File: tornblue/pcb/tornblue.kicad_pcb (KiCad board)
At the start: 2 copper layers, 140.7 x 102.9 mm, 80 parts, among them J1 BATT, J2 SWD, J3 BREAKOUT, J4 USB C - USB2.0, J5 BATT_PIN, Q1 AO3401A, Q2 AO3401A, SW1 SW_Push, SW10 SW_Push, SW11 SW_Push, SW12 SW_Push, SW13 SW_Push, SW14 SW_Push, SW15 SW_Push, SW16 SW_Push, SW17 SW_Push, SW18 SW_Push, SW19 EC11, SW2 SW_Push, SW20 SW_Push, SW21 SW_Push, SW22 EC11, SW23 RST, SW24 SW_SPST, SW3 SW_Push, SW4 SW_Push, SW5 SW_Push, SW6 SW_Push, SW7 SW_Push, SW8 SW_Push, SW9 SW_Push, U1 XC6220, U2 TP4056, U3 nRF52840_holyiot_18010, U4 SRV05-4

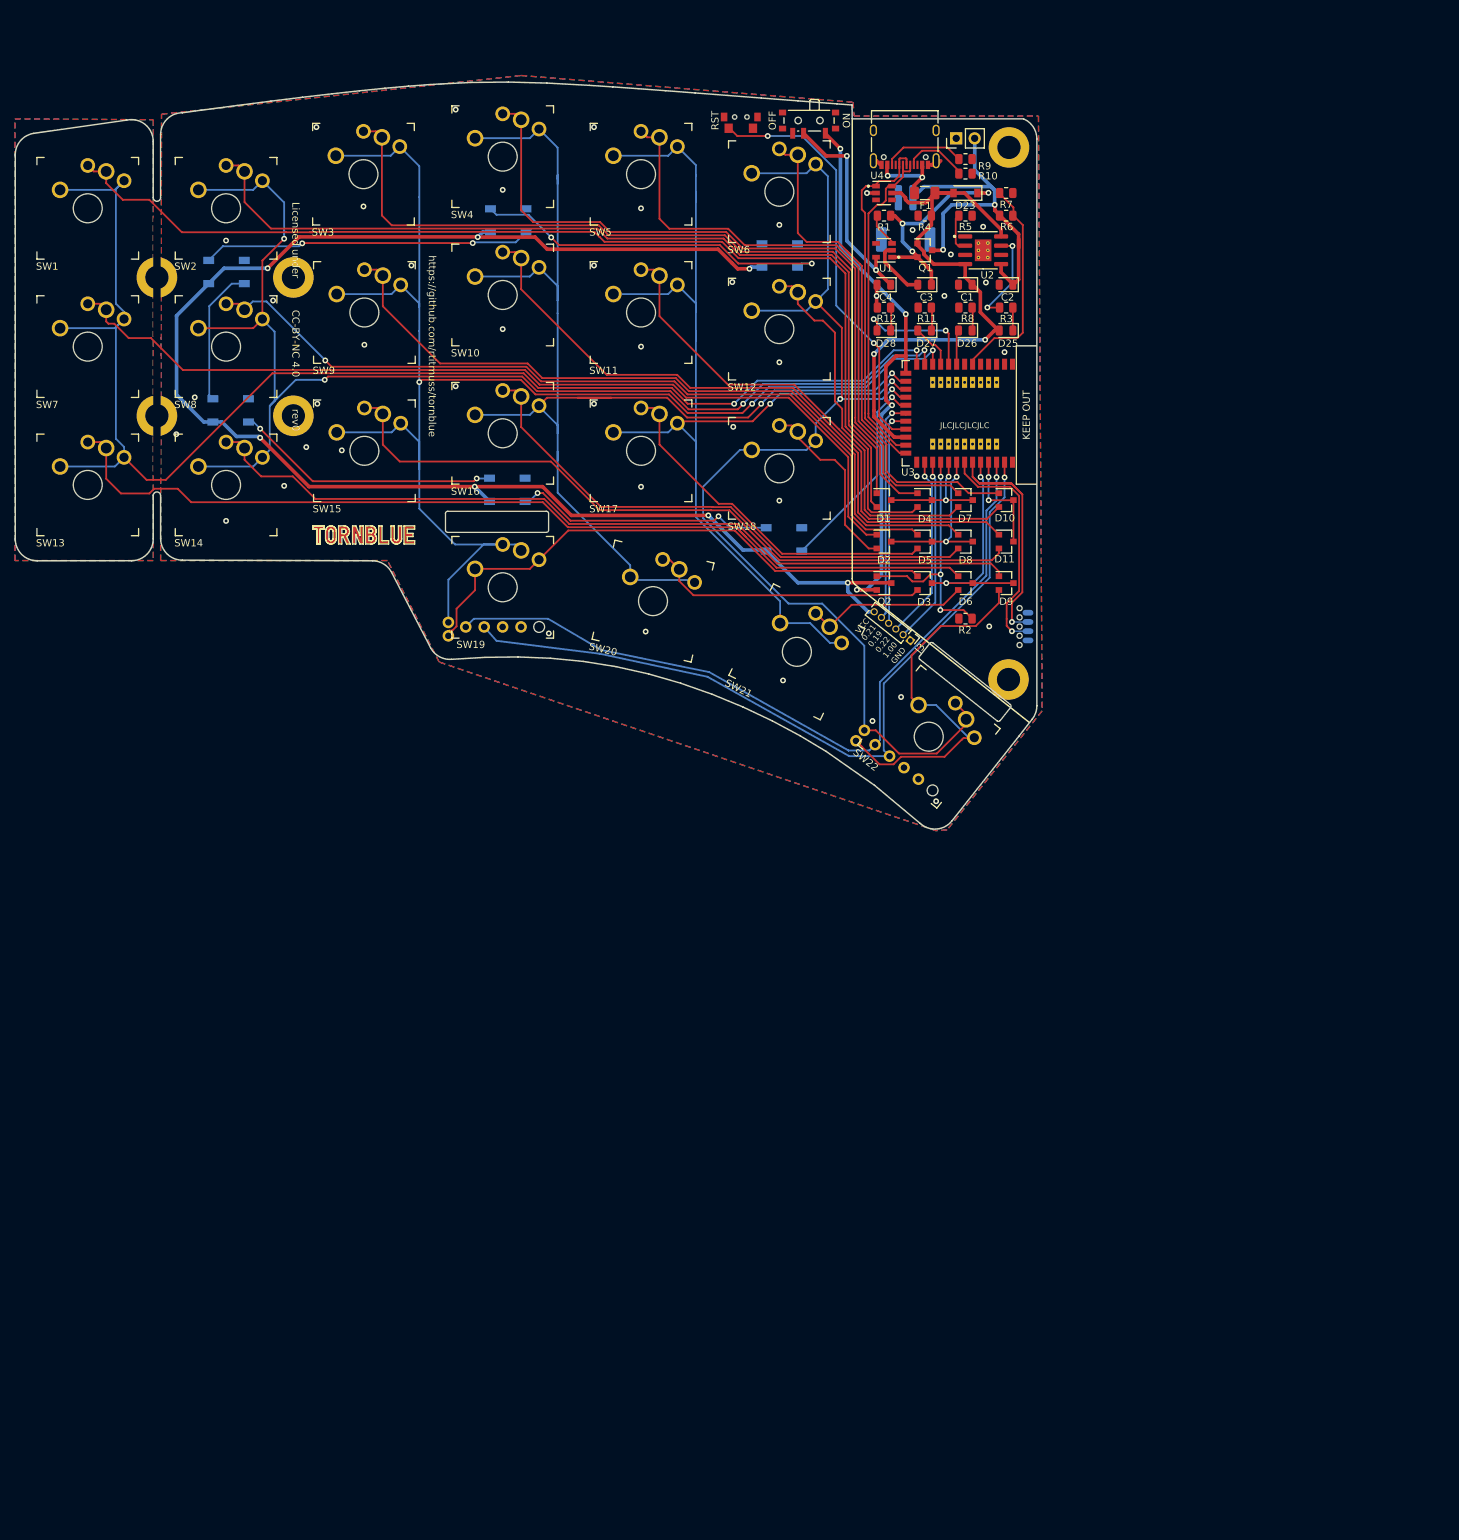
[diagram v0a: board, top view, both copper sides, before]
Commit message: Add right edgecuts
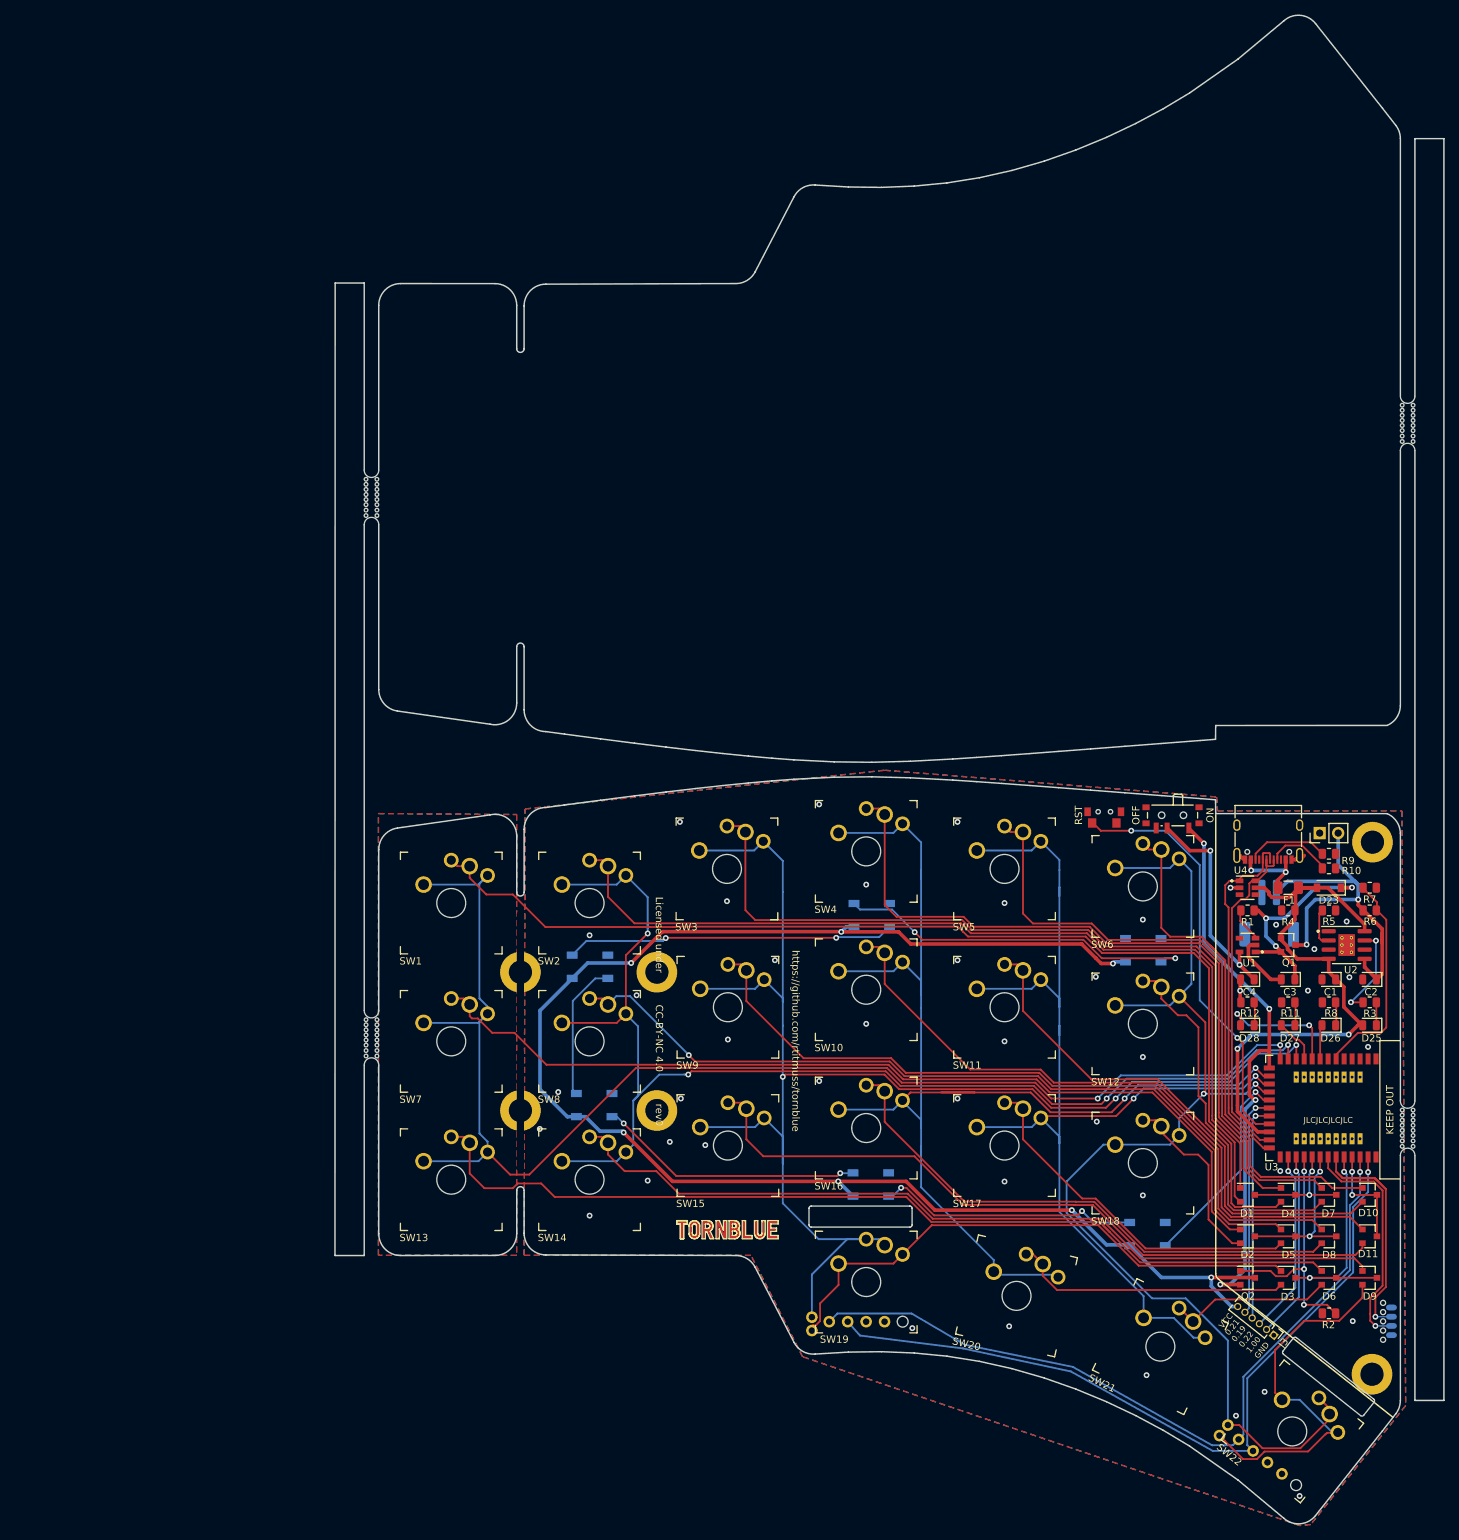
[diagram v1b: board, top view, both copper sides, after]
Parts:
- added mouse-bite-5mm-slot: VAL**, tornblue:mouse-bite-5mm-slot, F.Cu at (272.8, 94.3)
- added mouse-bite-5mm-slot: VAL**, tornblue:mouse-bite-5mm-slot, F.Cu at (272.8, 191.3)
- added mouse-bite-5mm-slot: VAL**, tornblue:mouse-bite-5mm-slot, F.Cu at (130.1, 104.5)
- added mouse-bite-5mm-slot: VAL**, tornblue:mouse-bite-5mm-slot, F.Cu at (130.1, 178.9)
- moved D3 108.0 mm to (256.4, 211.9)
- moved F1 108.0 mm to (256.4, 158.2)
- moved H1 108.0 mm to (268.0, 151.9)
- moved Q1 108.0 mm to (256.4, 166.1)
- moved R11 108.0 mm to (256.4, 174.0)
- moved D13 108.0 mm to (198.9, 199.1)
- moved D15 108.0 mm to (236.4, 166.8)
- moved D16 108.0 mm to (199.0, 162.0)
- moved D17 108.0 mm to (160.2, 169.1)
- moved D23 108.0 mm to (262.0, 158.2)
- moved D4 108.0 mm to (256.4, 200.5)
- moved D5 108.0 mm to (256.4, 206.2)
- moved D6 108.0 mm to (262.0, 211.9)
- moved D9 108.0 mm to (267.6, 211.9)
- moved H2 108.0 mm to (267.9, 225.2)
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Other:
- board size 140.7 x 102.9 mm -> 152.7 x 207.8 mm

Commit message: Add right schematic
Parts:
- added C5: 10uF, Diode_SMD:D_0805_2012Metric, F.Cu at (374.5, 130.2)
- added C6: 10uF, Diode_SMD:D_0805_2012Metric, F.Cu at (374.5, 133.2)
- added C7: 10uF, Diode_SMD:D_0805_2012Metric, F.Cu at (383.0, 125.3)
- added C8: 10uF, Diode_SMD:D_0805_2012Metric, F.Cu at (427.8, 79.5)
- added D18: BLUE, LED_SMD:LED_0805_2012Metric, F.Cu at (429.0, 75.2)
- added D19: BAV70_Small, Package_TO_SOT_SMD:SOT-23, F.Cu at (335.6, 133.9)
- added D20: BAV70_Small, Package_TO_SOT_SMD:SOT-23, F.Cu at (391.4, 116.4)
- added D21: BAV70_Small, Package_TO_SOT_SMD:SOT-23, F.Cu at (395.9, 111.8)
- added D22: BAV70_Small, Package_TO_SOT_SMD:SOT-23, F.Cu at (410.5, 96.5)
- added D24: B5819W, Diode_SMD:D_SOD-123, F.Cu at (306.3, 133.3)
- added D29: BAV70_Small, Package_TO_SOT_SMD:SOT-23, F.Cu at (415.0, 92.0)
- added D30: BAV70_Small, Package_TO_SOT_SMD:SOT-23, F.Cu at (417.5, 87.4)
- added D31: BAV70_Small, Package_TO_SOT_SMD:SOT-23, F.Cu at (410.5, 92.0)
- added D32: BAV70_Small, Package_TO_SOT_SMD:SOT-23, F.Cu at (391.4, 111.8)
- added D33: BAV70_Small, Package_TO_SOT_SMD:SOT-23, F.Cu at (370.0, 131.0)
- added D34: BAV70_Small, Package_TO_SOT_SMD:SOT-23, F.Cu at (383.0, 118.5)
- added D35: BAV70_Small, Package_TO_SOT_SMD:SOT-23, F.Cu at (340.1, 133.9)
- added D36: WS2812B, LED_SMD:LED_WS2812B_PLCC4_5.0x5.0mm_P3.2mm, F.Cu at (385.0, 112.9)
- added D37: WS2812B, LED_SMD:LED_WS2812B_PLCC4_5.0x5.0mm_P3.2mm, F.Cu at (363.6, 132.0)
- added D38: WS2812B, LED_SMD:LED_WS2812B_PLCC4_5.0x5.0mm_P3.2mm, F.Cu at (422.6, 74.6)
- added D39: WS2812B, LED_SMD:LED_WS2812B_PLCC4_5.0x5.0mm_P3.2mm, F.Cu at (355.1, 132.0)
- added D40: WS2812B, LED_SMD:LED_WS2812B_PLCC4_5.0x5.0mm_P3.2mm, F.Cu at (346.7, 132.0)
- added D41: WS2812B, LED_SMD:LED_WS2812B_PLCC4_5.0x5.0mm_P3.2mm, F.Cu at (404.1, 93.8)
- added D42: GREEN, LED_SMD:LED_0805_2012Metric, F.Cu at (402.1, 103.9)
- added D43: GREEN, LED_SMD:LED_0805_2012Metric, F.Cu at (383.0, 122.3)
- added D44: GREEN, LED_SMD:LED_0805_2012Metric, F.Cu at (370.0, 134.8)
- added F2: 750mA, Fuse:Fuse_1206_3216Metric, F.Cu at (312.0, 133.2)
- added H10: MountingHole, MountingHole:MountingHole_3.2mm_M3_DIN965_Pad, F.Cu at (430.8, 63.0)
- added H11: MountingHole, tornblue:MountingHole_3.2mm_M3_DIN965_Pad_Slot, F.Cu at (288.8, 86.9)
- added H12: MountingHole, tornblue:MountingHole_3.2mm_M3_DIN965_Pad_Slot, F.Cu at (288.8, 63.8)
- added H7: MountingHole, MountingHole:MountingHole_3.2mm_M3_DIN965_Pad, F.Cu at (430.8, 70.1)
- added H8: MountingHole, MountingHole:MountingHole_3.2mm_M3_DIN965_Pad, F.Cu at (422.0, 81.5)
- added H9: MountingHole, MountingHole:MountingHole_3.2mm_M3_DIN965_Pad, F.Cu at (411.7, 86.1)
- added J10: USB C - USB2.0, Connector_USB:USB_C_Receptacle_XKB_U262-16XN-4BVC11, F.Cu at (291.0, 124.3)
- added J6: BATT, Connector_JST:JST_PH_S2B-PH-SM4-TB_1x02-1MP_P2.00mm_Horizontal, F.Cu at (413.3, 76.9)
- added J7: BATT_PIN, Connector_PinHeader_2.54mm:PinHeader_1x02_P2.54mm_Vertical, F.Cu at (429.6, 54.5)
- added J8: BREAKOUT, Connector_PinHeader_1.27mm:PinHeader_1x06_P1.27mm_Vertical, F.Cu at (298.9, 120.7)
- added J9: SWD, tornblue:SOIC_clipProgSmall, F.Cu at (296.8, 96.4)
- added Q3: AO3401A, Package_TO_SOT_SMD:SOT-23, F.Cu at (331.2, 133.9)
- added Q4: AO3401A, Package_TO_SOT_SMD:SOT-23, F.Cu at (326.7, 133.9)
- added R13: 1k, Resistor_SMD:R_0805_2012Metric, F.Cu at (400.3, 111.0)
- added R14: 10k, Resistor_SMD:R_0805_2012Metric, F.Cu at (408.6, 100.3)
- added R15: 100k, Resistor_SMD:R_0805_2012Metric, F.Cu at (419.4, 91.1)
- added R16: 100k, Resistor_SMD:R_0805_2012Metric, F.Cu at (378.9, 130.2)
- added R17: 2M, Resistor_SMD:R_0805_2012Metric, F.Cu at (387.4, 123.1)
- added R18: 1k, Resistor_SMD:R_0805_2012Metric, F.Cu at (387.4, 120.1)
- added R19: 1k, Resistor_SMD:R_0805_2012Metric, F.Cu at (402.1, 106.9)
- added R20: 1k, Resistor_SMD:R_0805_2012Metric, F.Cu at (406.5, 103.9)
- added R21: 806k, Resistor_SMD:R_0805_2012Metric, F.Cu at (427.7, 82.5)
- added R22: 2M, Resistor_SMD:R_0805_2012Metric, F.Cu at (415.0, 95.7)
- added R23: 5.1k, Resistor_SMD:R_0805_2012Metric, F.Cu at (421.9, 86.6)
- added R24: 5.1k, Resistor_SMD:R_0805_2012Metric, F.Cu at (395.8, 115.6)
- added SW25: SW_Push, tornblue:MX_PG1350_optional, F.Cu at (360.3, 80.9)
- added SW26: SW_Push, tornblue:MX_PG1350_optional, F.Cu at (313.8, 102.9)
- added SW27: SW_Push, tornblue:MX_PG1350_optional, F.Cu at (341.2, 80.9)
- added SW28: EC11, tornblue:MX_PG1350_EVQWGD001_LR_optional, F.Cu at (294.7, 109.5)
- added SW29: SW_Push, tornblue:MX_PG1350_optional, F.Cu at (360.3, 61.8)
- added SW30: SW_Push, tornblue:MX_PG1350_optional, F.Cu at (341.2, 61.8)
- added SW31: SW_Push, tornblue:MX_PG1350_optional, F.Cu at (321.1, 83.8)
- added SW32: SW_Push, tornblue:MX_PG1350_optional, F.Cu at (302.0, 83.8)
- added SW33: SW_Push, tornblue:MX_PG1350_optional, F.Cu at (333.0, 102.9)
- added SW34: SW_Push, tornblue:MX_PG1350_optional, F.Cu at (313.8, 122.0)
- added SW35: SW_Push, tornblue:MX_PG1350_optional, F.Cu at (379.4, 61.8)
- added SW36: SW_Push, tornblue:MX_PG1350_optional, F.Cu at (352.1, 100.0)
- added SW37: SW_Push, tornblue:MX_PG1350_optional, F.Cu at (390.3, 100.0)
- added SW38: SW_Push, tornblue:MX_PG1350_optional, F.Cu at (398.6, 80.9)
- added SW39: SW_Push, tornblue:MX_PG1350_optional, F.Cu at (371.2, 100.0)
- added SW40: SW_Push, tornblue:MX_PG1350_optional, F.Cu at (352.1, 119.1)
- added SW41: SW_Push, tornblue:MX_PG1350_optional, F.Cu at (398.6, 61.8)
- added SW42: SW_Push, tornblue:MX_PG1350_optional, F.Cu at (379.4, 80.9)
- added SW43: SW_Push, tornblue:MX_PG1350_optional, F.Cu at (333.0, 122.0)
- added SW44: SW_SPST, Button_Switch_SMD:SW_SPDT_PCM12, F.Cu at (290.1, 132.0)
- added SW45: EC11, tornblue:MX_PG1350_EVQWGD001_LR_optional, F.Cu at (322.1, 63.2)
- added SW46: SW_Push, tornblue:MX_PG1350_optional, F.Cu at (371.2, 119.1)
- added SW47: SW_Push, tornblue:MX_PG1350_optional, F.Cu at (417.7, 61.8)
- added SW48: RESET, tornblue:SW_SPST_TS24CA, F.Cu at (403.1, 99.7)
- added U5: TP4056, Package_SO:SOIC-8-1EP_3.9x4.9mm_P1.27mm_EP2.29x3mm_ThermalVias, F.Cu at (299.2, 132.2)
- added U6: XC6220, Package_TO_SOT_SMD:SOT-23-5, F.Cu at (317.2, 133.9)
- added U7: SRV05-4, Package_TO_SOT_SMD:SOT-23-6, F.Cu at (322.1, 133.9)
- added U8: nRF52840_holyiot_18010, kicad-keyboard-parts:nRF52840_holyiot_18010, F.Cu at (302.5, 64.0)
- SW23: value RST -> RESET

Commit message: Placed components on the right side
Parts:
- D36, D37, D38, D39, D40, D41, J6, J9: moved to B.Cu
- moved H10 266.3 mm to (169.4, 114.0)
- moved D38 262.6 mm to (160.8, 95.7)
- moved H7 262.6 mm to (169.4, 94.9)
- moved SW37 249.6 mm to (141.1, 85.4), turned to 180 degrees
- moved D41 244.8 mm to (160.2, 114.7)
- moved SW38 238.4 mm to (160.2, 85.4), turned to 180 degrees
- moved SW25 223.3 mm to (141.1, 123.5), turned to 180 degrees
- moved SW39 192.4 mm to (179.1, 90.0), turned to 180 degrees
- moved J7 186.2 mm to (260.7, 133.1), turned to 90 degrees
- moved SW41 183.4 mm to (217.3, 90.1), turned to 180 degrees
- moved SW31 181.1 mm to (141.1, 104.4), turned to 180 degrees
- moved C8 180.1 mm to (250.8, 113.0)
- moved SW45 178.9 mm to (238.8, 62.4), turned to 206 degrees
- moved SW48 175.9 mm to (231.1, 136.1), turned to 180 degrees
- moved D37 171.3 mm to (198.9, 84.7)
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- renumbered SW43 to SW28, SW28 to SW43, SW46 to SW44, SW47 to SW45, SW45 to SW46, SW44 to SW47
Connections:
- C5 pad 1: +5V -> +5VP
- C5 pad 2: GND -> GND1
- C6 pad 2: GND -> GND1
- C7 pad 2: GND -> GND1
- C8 pad 2: GND -> GND1
- D18 pad 2: +5V -> +5VP
- D24 pad 2: +5V -> +5VP
- D36 pad 3: GND -> GND1
- D37 pad 3: GND -> GND1
- D38 pad 3: GND -> GND1
- D39 pad 3: GND -> GND1
- D40 pad 3: GND -> GND1
- D41 pad 3: GND -> GND1
- F2 pad 1: +5V -> +5VP
- F2 pad 2: VBUS -> VBUS_R
- J10 pad A1: GND -> GND1
- J10 pad A12: GND -> GND1
- J10 pad A4: VBUS -> VBUS_R
- J10 pad A9: VBUS -> VBUS_R
- J10 pad B1: GND -> GND1
- J10 pad B12: GND -> GND1
- J10 pad B4: VBUS -> VBUS_R
- J10 pad B9: VBUS -> VBUS_R
- J10 pad S1: GND -> GND1
- J6 pad 2: GND -> GND1
- J7 pad 1: GND -> GND1
- J8 pad 1: GND -> GND1
- J9 pad 1: GND -> GND1
- Q3 pad 1: +5V -> +5VP
- Q4 pad 2: +3V3 -> +3.3VP
- R14 pad 1: GND -> GND1
- R15 pad 1: +5V -> +5VP
- R15 pad 2: GND -> GND1
- R17 pad 1: GND -> GND1
- R18 pad 2: GND -> GND1
- R19 pad 2: GND -> GND1
- R20 pad 2: GND -> GND1
- R22 pad 2: GND -> GND1
- R23 pad 1: GND -> GND1
- R24 pad 1: GND -> GND1
- SW43 pad C: GND -> GND1
- SW46 pad C: GND -> GND1
- SW47 pad 1: +3V3 -> +3.3VP
- SW48 pad 2: GND -> GND1
- U5 pad 1: GND -> GND1
- U5 pad 3: GND -> GND1
- U5 pad 4: +5V -> +5VP
- U5 pad 8: +5V -> +5VP
- U6 pad 2: GND -> GND1
- U7 pad 2: GND -> GND1
- U7 pad 5: +5V -> +5VP
- U8 pad 1: GND -> GND1
- U8 pad 14: +3V3 -> +3.3VP
- U8 pad 22: +5V -> +5VP
- U8 pad 25: GND -> GND1
- U8 pad 37: GND -> GND1
